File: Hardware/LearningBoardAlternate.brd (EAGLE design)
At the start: 90.9 x 91.4 mm, 55 parts, among them IC1 FT230XS-RFT230XS-R

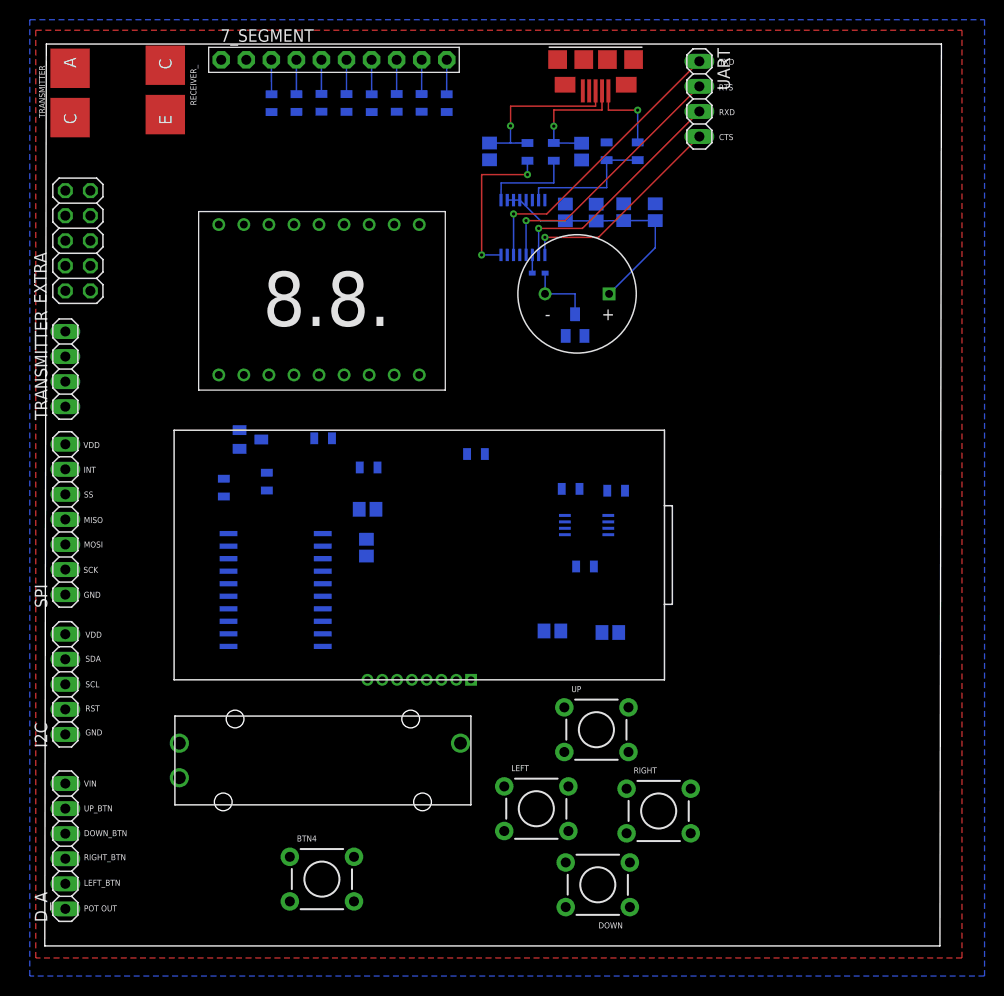
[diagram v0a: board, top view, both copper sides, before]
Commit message: Finished the alternate PCB design
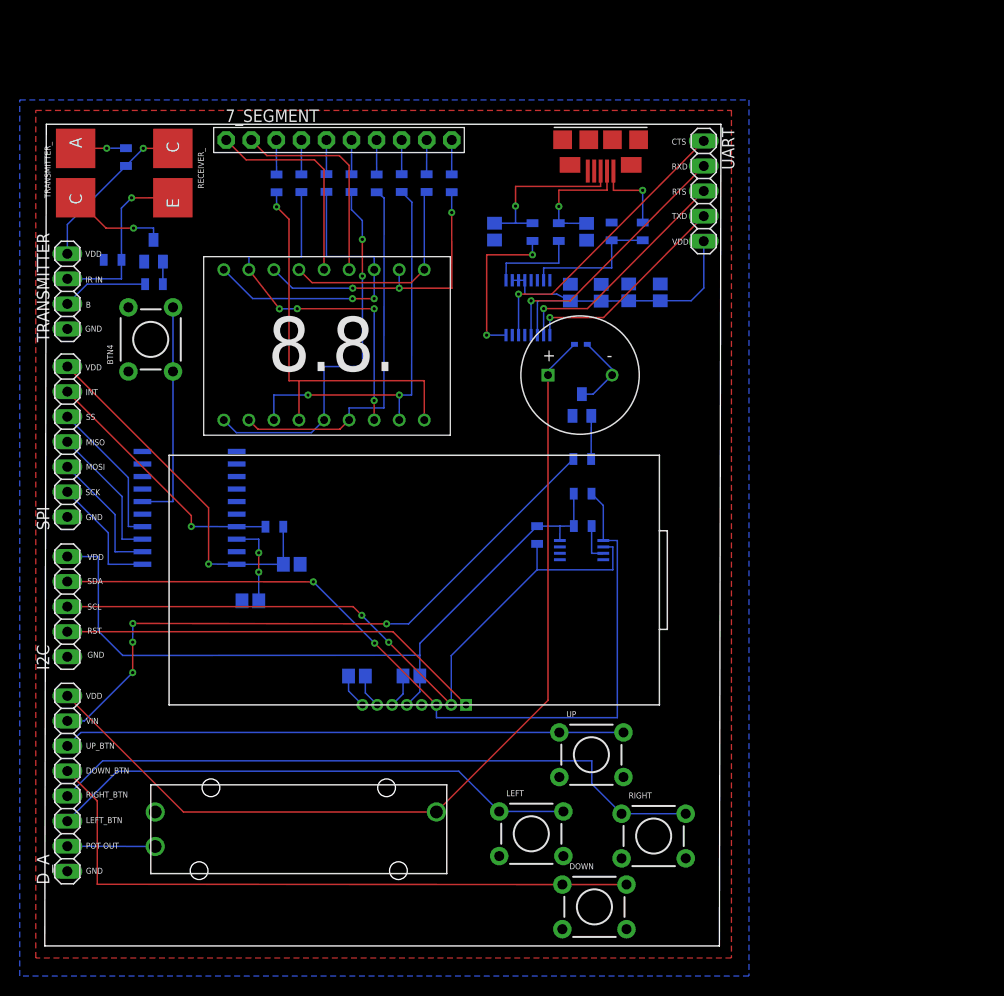
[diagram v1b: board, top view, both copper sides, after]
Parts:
- removed EXTRA: (no value), pinhead:2X05
- D_A: device pinhead:1X06 -> pinhead:1X08
- UART: device pinhead:1X04 -> pinhead:1X05
- moved BTN4 57.4 mm to (10.7, 61.5), turned to 90 degrees
- moved RPU12 34.9 mm to (8.23, 80.0)
- moved RPU14 27.4 mm to (6.87, 69.5), turned to 0 degrees
- moved RPU13 23.2 mm to (11.1, 67.1)
- moved T1 21.5 mm to (11.0, 70.5), turned to 0 degrees
- moved C1 20.6 mm to (37.2, 27.4)
- moved C2 20.3 mm to (31.6, 27.4)
- moved C4 12.9 mm to (20.8, 35.0), turned to 0 degrees
- moved U$1 12.1 mm to (14.7, 44.4), turned to 180 degrees
- moved RPU4 11.3 mm to (23.3, 42.5)
- moved RPU15 10.8 mm to (54.5, 49.4)
- moved C3 9.50 mm to (25.0, 38.7), turned to 180 degrees
- moved UART 9.35 mm to (66.8, 76.5)
- moved RECEIVER_ 8.47 mm to (13.0, 78.3)
- moved U$9 8.40 mm to (54.3, 61.0)
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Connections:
- net N$28 renamed BASE
- new net VDD_I2C: C1.1, I2C.5, RPU16.2, RPU17.2, RPU5.1, U$11.8, U$2.5
- new net VDD_IR: RECEIVER_.C, RPU12.2, TRANSMITTER.4
- new net VDD_SPI: C3.1, RPU4.1, SPI.7, U$1.20
- new net VDD_UART: C10.1, C5.1, C8.1, C9.1, IC1.10, IC1.11, IC1.12, IC1.3, UART.5
- net DOWN_BTN: now also D_A.5; no longer D_A.4
- net LEFT_BTN: now also D_A.3; no longer D_A.2
- net POT_OUT: now also D_A.2; no longer D_A.1
- net RIGHT_BTN: now also D_A.4; no longer D_A.3
- net UP_BTN: now also D_A.6; no longer D_A.5
- net VDD: now also D_A.8; no longer C1.1, C10.1, C3.1, C5.1, C8.1, C9.1, EXTRA.10, EXTRA.2, EXTRA.4, EXTRA.6, EXTRA.8, I2C.5, IC1.10, IC1.11, IC1.12, IC1.3, RECEIVER_.C, RPU12.2, RPU16.2, RPU17.2, RPU4.1, RPU5.1, SPI.7, TRANSMITTER.4, U$1.20, U$11.8, U$2.5
- net VIN: now also D_A.7; no longer D_A.6
- net VSS: now also D_A.1; no longer EXTRA.1, EXTRA.3, EXTRA.5, EXTRA.7, EXTRA.9
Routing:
- net SDA: track 0.00 -> 86.8 mm, vias 0 -> 2
- net VDD_I2C: track 0.00 -> 76.4 mm
- net SCL: track 0.00 -> 73.9 mm, vias 0 -> 2
- net VDD: track 27.1 -> 95.5 mm
- net RIGHT_BTN: track 0.00 -> 67.8 mm
- net DOWN_BTN: track 0.00 -> 66.4 mm
- net VIN: track 0.00 -> 65.2 mm, vias 0 -> 4
- net UP_BTN: track 0.00 -> 56.9 mm
- net LEFT_BTN: track 0.00 -> 54.1 mm
- net RST: track 0.00 -> 43.5 mm
- net N$13: track 0.00 -> 41.3 mm, vias 0 -> 1
- net N$9: track 0.00 -> 40.0 mm, vias 0 -> 2
- net N$12: track 0.00 -> 39.1 mm, vias 0 -> 4
- net N$10: track 0.00 -> 38.7 mm, vias 0 -> 2
- net N$8: track 0.00 -> 37.9 mm
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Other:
- board size 90.9 x 91.4 mm -> 68.5 x 83.3 mm
- board text added: "B"
- board text added: "IR IN"

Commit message: Updated parts on board and part labels
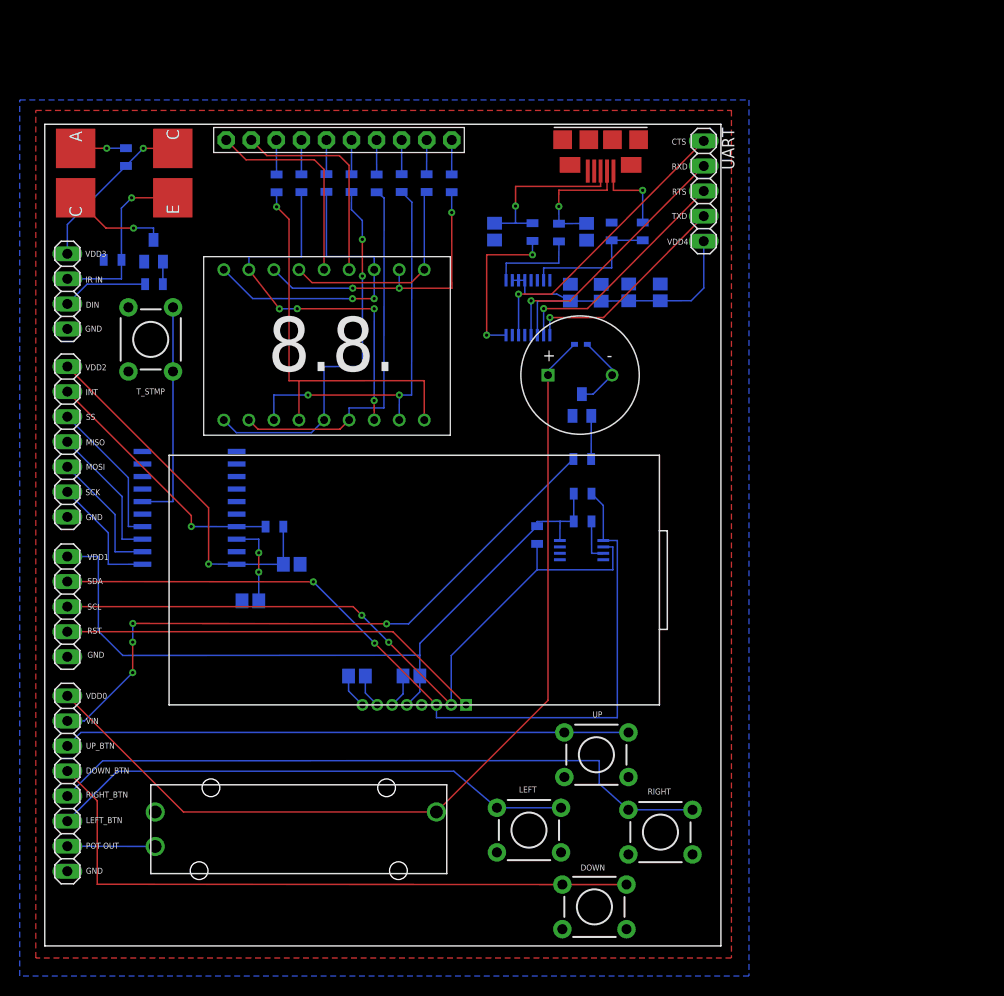
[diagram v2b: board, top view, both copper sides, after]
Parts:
- moved RIGHT 0.80 mm to (62.4, 11.5)
- moved UP 0.51 mm to (55.9, 19.4)
- moved RPU5 0.47 mm to (54.5, 43.0)
- moved LEFT 0.44 mm to (49.1, 11.7)
- moved RPU6 0.06 mm to (52.1, 72.3)
- renumbered BTN4 to T_STMP
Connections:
- net BASE renamed DIN
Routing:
- net LEFT_BTN: track 54.1 -> 53.5 mm
- net UP_BTN: track 56.9 -> 57.4 mm
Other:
- outline, holes or cut-outs redrawn
- board text added: "DIN"
- board text added: "VDD0"
- board text added: "VDD1"
- board text added: "VDD2"
- board text added: "VDD3"
- board text added: "VDD4"
- board text removed: "B"
- board text removed: "VDD"
